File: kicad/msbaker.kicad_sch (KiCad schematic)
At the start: 37 parts, among them J1 USB_B_Micro, J2 Micro_SD_Card, J3 GPIO, U1 MIC5365-3.3YC5, U2 W25Q128JVS, U3 RP2040, U4 LSM6DSO32, Y1 12MHz

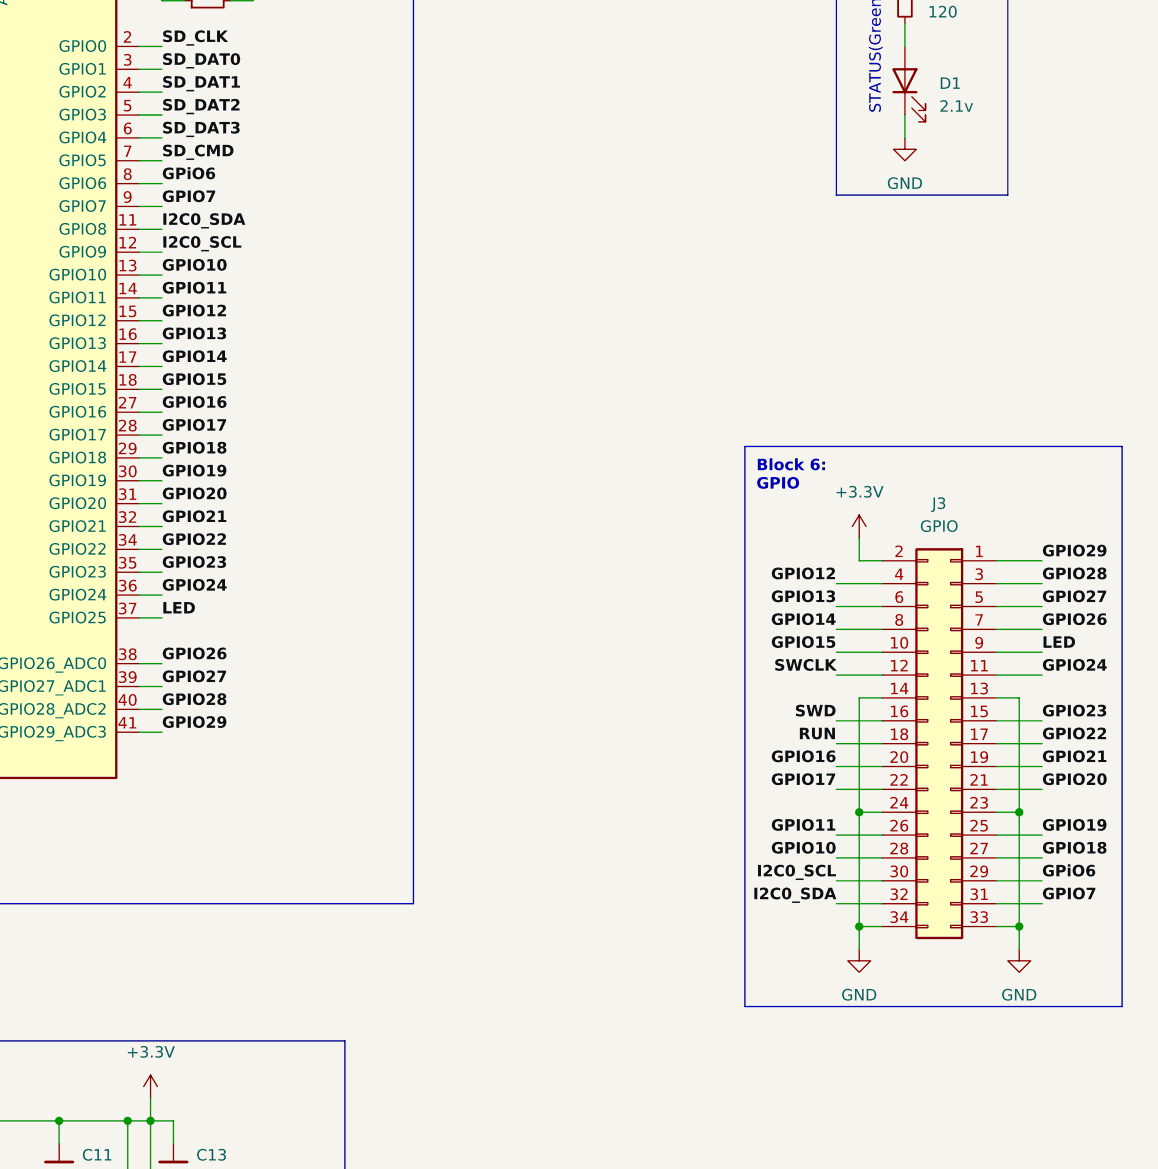
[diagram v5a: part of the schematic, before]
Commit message: Corrected small mistake where I2C0 was placed on GPIO8 and GPIO9 instead of chip pin 8 and 9
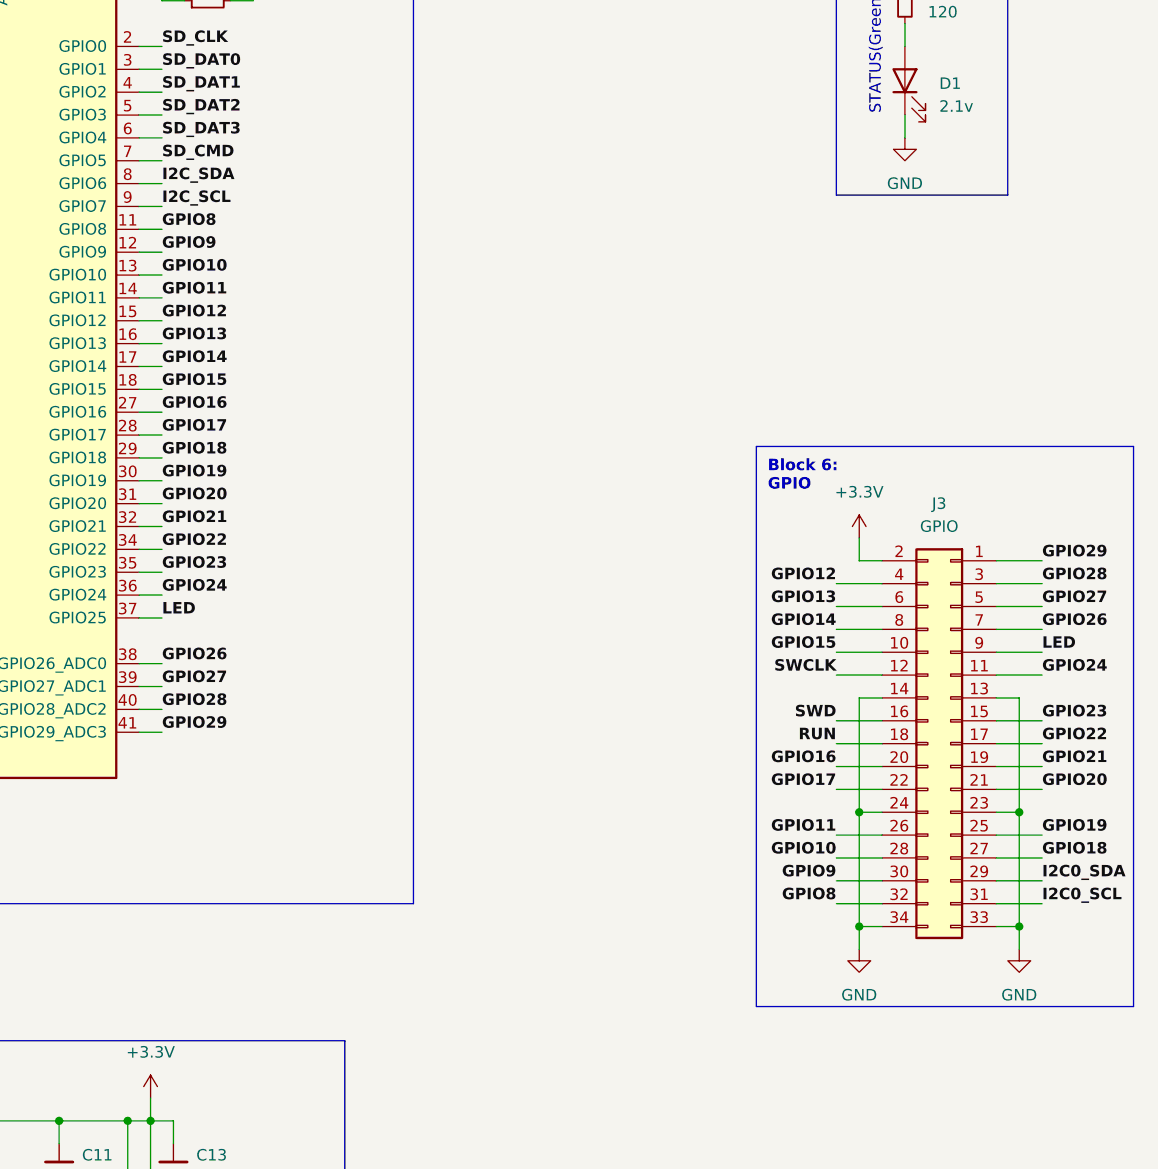
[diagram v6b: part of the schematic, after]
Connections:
- net I2C0_SCL: now also J3.31 (Pin_31); no longer J3.30 (Pin_30), U3.12 (GPIO9)
- net I2C0_SDA: now also J3.29 (Pin_29); no longer J3.32 (Pin_32), U3.11 (GPIO8)
- net I2C_SCL: now also U3.9 (GPIO7)
- removed net GPIO7: J3.31 (Pin_31), U3.9 (GPIO7)
- net GPiO6 renamed I2C_SDA
- net I2C_SDA: no longer J3.29 (Pin_29)
- new net GPIO8: J3.32 (Pin_32), U3.11 (GPIO8)
- new net GPIO9: J3.30 (Pin_30), U3.12 (GPIO9)
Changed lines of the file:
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@@
     (stroke (width 0) (type default) (color 0 0 0 0))
   )
-  (polyline (pts (xy 363.22 207.01) (xy 363.22 144.78))
+  (polyline (pts (xy 364.49 207.01) (xy 364.49 144.78))
     (stroke (width 0) (type default) (color 0 0 0 0))
   )
@@
     (stroke (width 0) (type default) (color 0 0 0 0))
   )
-  (polyline (pts (xy 321.31 144.78) (xy 363.22 144.78))
+  (polyline (pts (xy 322.58 144.78) (xy 364.49 144.78))
     (stroke (width 0) (type default) (color 0 0 0 0))
   )
@@
     (stroke (width 0) (type default) (color 0 0 0 0))
   )
-  (polyline (pts (xy 321.31 207.01) (xy 363.22 207.01))
+  (polyline (pts (xy 322.58 207.01) (xy 364.49 207.01))
     (stroke (width 0) (type default) (color 0 0 0 0))
   )
@@
     (stroke (width 0) (type default) (color 0 0 0 0))
   )
-  (polyline (pts (xy 321.31 144.78) (xy 321.31 207.01))
+  (polyline (pts (xy 322.58 144.78) (xy 322.58 207.01))
     (stroke (width 0) (type default) (color 0 0 0 0))
   )
@@
     (effects (font (size 1.27 1.27) bold) (justify left bottom))
   )
-  (text "Block 6:\nGPIO" (at 322.58 149.86 0)
+  (text "Block 6:\nGPIO" (at 323.85 149.86 0)
     (effects (font (size 1.27 1.27) bold) (justify left bottom))
   )
@@
     (effects (font (size 1.27 1.27) bold) (justify right bottom))
   )
-  (label "GPiO6" (at 354.33 193.04 0)
-    (effects (font (size 1.27 1.27) bold) (justify left bottom))
-  )
-  (label "GPIO7" (at 354.33 195.58 0)
+  (label "I2C0_SDA" (at 354.33 193.04 0)
+    (effects (font (size 1.27 1.27) bold) (justify left bottom))
+  )
+  (label "I2C0_SCL" (at 354.33 195.58 0)
     (effects (font (size 1.27 1.27) bold) (justify left bottom))
   )
@@
     (effects (font (size 1.27 1.27) bold) (justify left bottom))
   )
-  (label "I2C0_SCL" (at 331.47 193.04 180)
-    (effects (font (size 1.27 1.27) bold) (justify right bottom))
-  )
-  (label "GPIO7" (at 256.54 118.11 0)
+  (label "GPIO9" (at 331.47 193.04 180)
+    (effects (font (size 1.27 1.27) bold) (justify right bottom))
+  )
+  (label "I2C_SCL" (at 256.54 118.11 0)
     (effects (font (size 1.27 1.27) bold) (justify left bottom))
   )
@@
     (effects (font (size 1.27 1.27) bold) (justify left bottom))
   )
-  (label "GPiO6" (at 256.54 115.57 0)
+  (label "I2C_SDA" (at 256.54 115.57 0)
     (effects (font (size 1.27 1.27) bold) (justify left bottom))
   )
@@
     (effects (font (size 1.27 1.27) bold) (justify left bottom))
   )
-  (label "I2C0_SCL" (at 256.54 123.19 0)
+  (label "GPIO9" (at 256.54 123.19 0)
     (effects (font (size 1.27 1.27) bold) (justify left bottom))
   )
@@
     (effects (font (size 1.27 1.27) bold) (justify left bottom))
   )
-  (label "I2C0_SDA" (at 256.54 120.65 0)
+  (label "GPIO8" (at 256.54 120.65 0)
     (effects (font (size 1.27 1.27) bold) (justify left bottom))
   )
@@
     (effects (font (size 1.27 1.27) bold) (justify right bottom))
   )
-  (label "I2C0_SDA" (at 331.47 195.58 180)
-    (effects (font (size 1.27 1.27) bold) (justify right bottom))
-  )
+  (label "GPIO8" (at 331.47 195.58 180)
+    (effects (font (size 1.27 1.27) bold) (justify right bottom))
+  )
